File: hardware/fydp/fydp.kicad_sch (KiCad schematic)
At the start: 0 parts

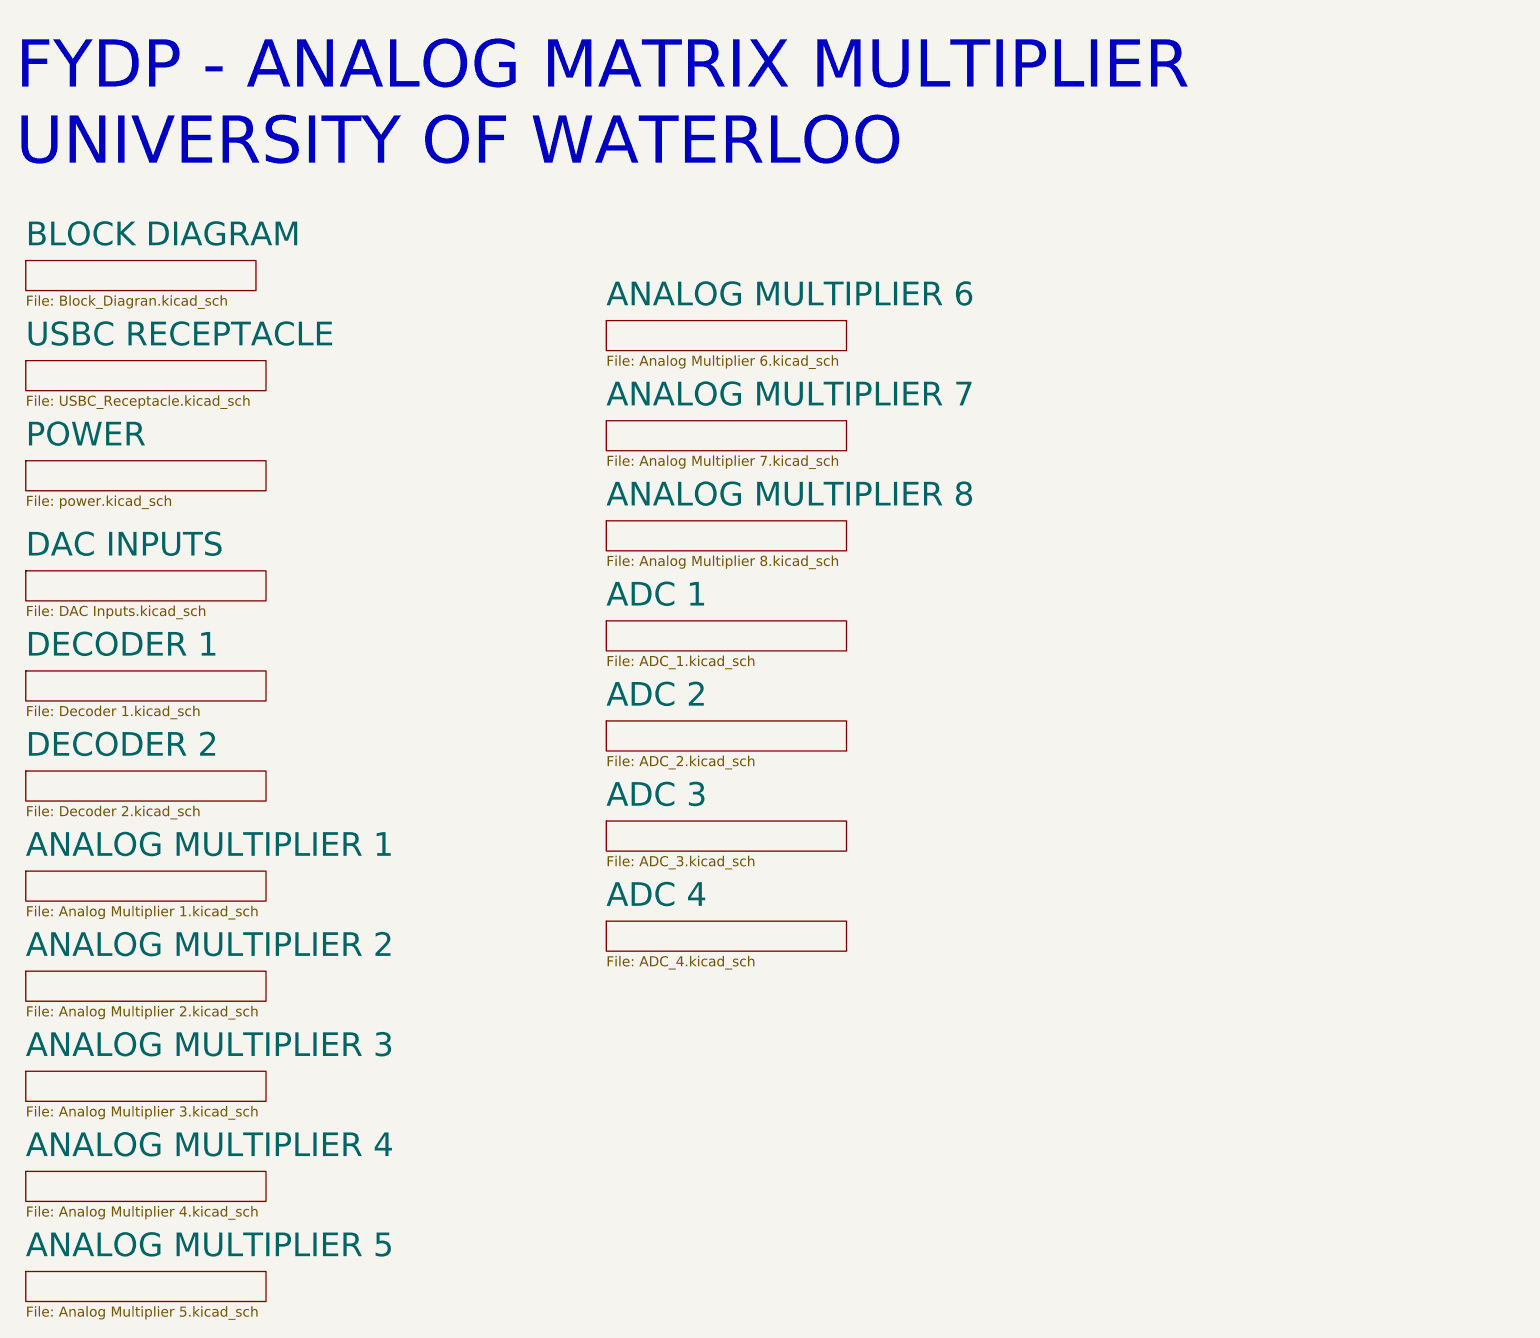
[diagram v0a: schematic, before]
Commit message: Remove 2 channels of multiplier and change ADC
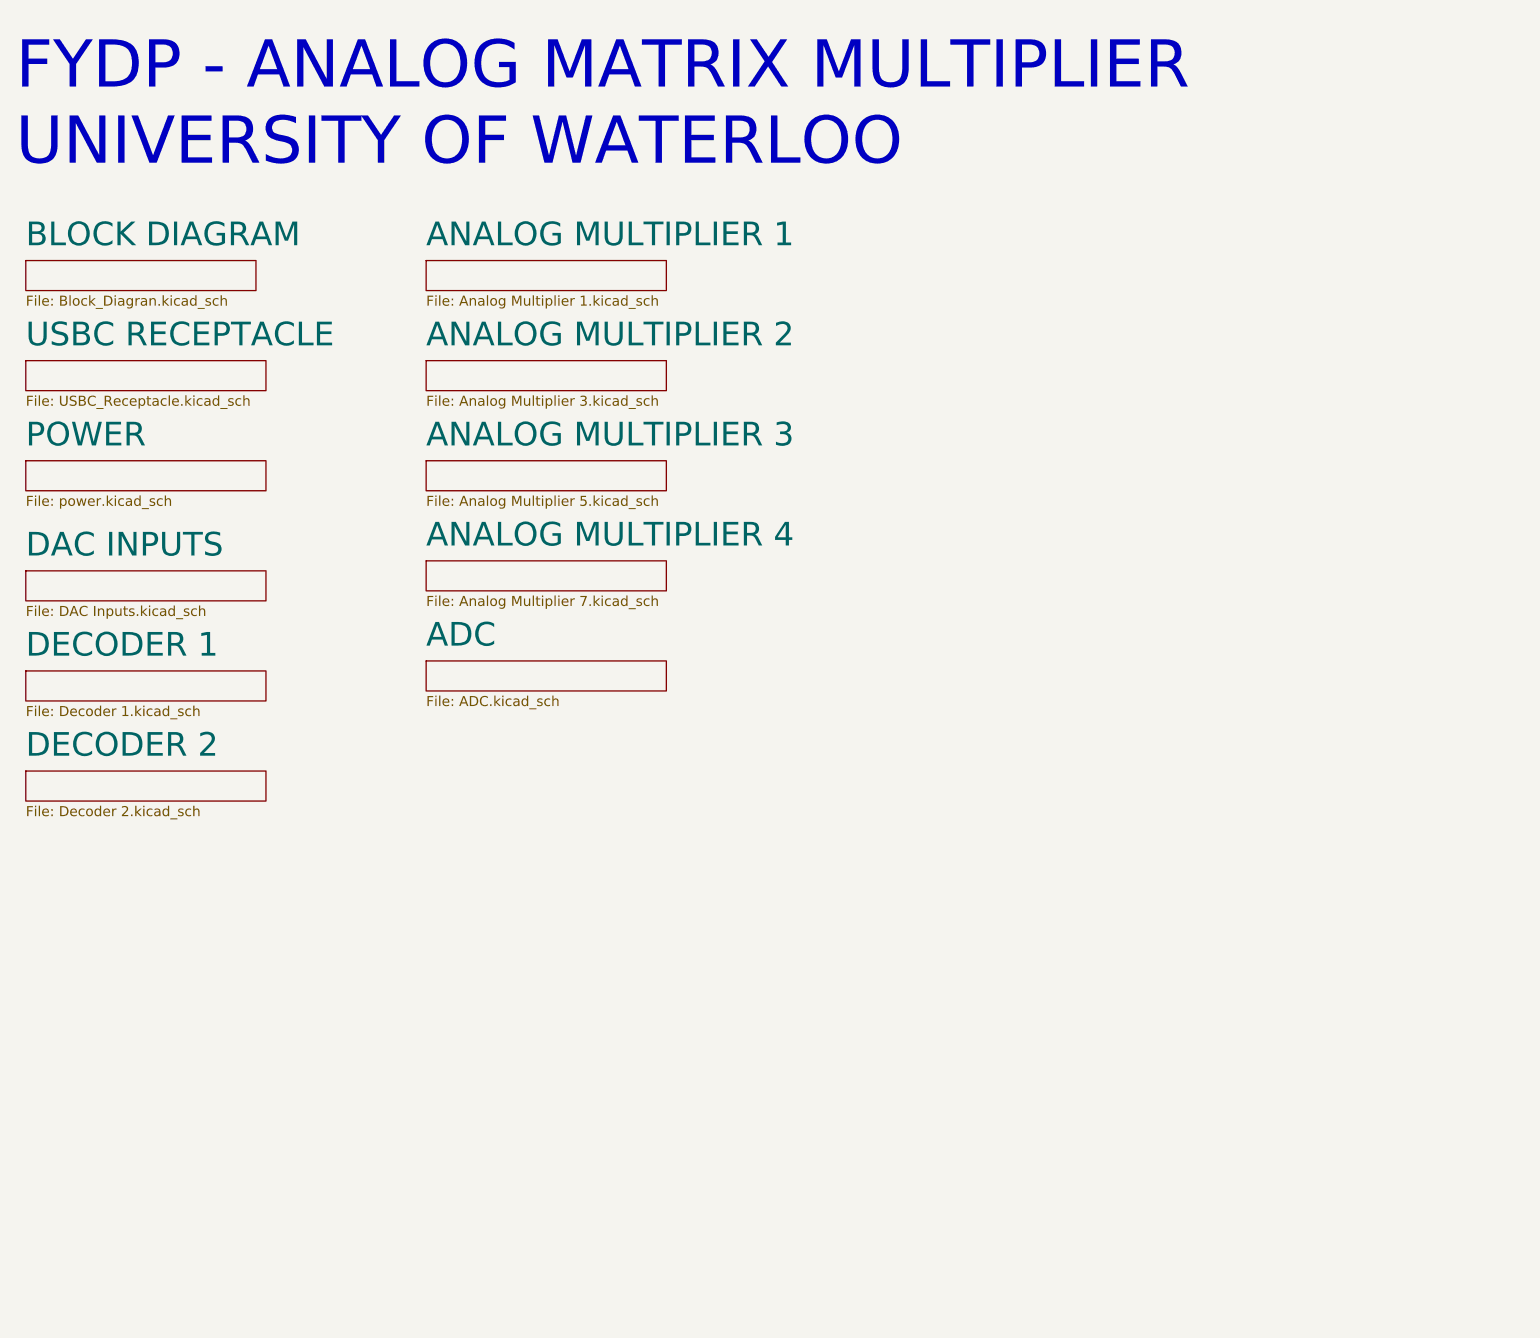
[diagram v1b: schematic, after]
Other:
- removed sheet ADC 1
- removed sheet ADC 2
- removed sheet ADC 3
- removed sheet ADC 4
- removed sheet ANALOG MULTIPLIER 5
- removed sheet ANALOG MULTIPLIER 6
- removed sheet ANALOG MULTIPLIER 7
- removed sheet ANALOG MULTIPLIER 8
- added sheet ADC (ADC.kicad_sch)
- sheet ANALOG MULTIPLIER 2: file Analog Multiplier 2.kicad_sch -> Analog Multiplier 3.kicad_sch
- sheet ANALOG MULTIPLIER 3: file Analog Multiplier 3.kicad_sch -> Analog Multiplier 5.kicad_sch
- sheet ANALOG MULTIPLIER 4: file Analog Multiplier 4.kicad_sch -> Analog Multiplier 7.kicad_sch
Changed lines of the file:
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@@
     (effects (font (size 6 6)) (justify left bottom))
-  )
-  (sheet (at 104.14 85.09) (size 30.48 3.81) (fields_autoplaced)
-    (stroke (width 0.1524) (type solid))
-    (fill (color 0 0 0 0.0000))
-    (property "Sheetname" "ANALOG MULTIPLIER 8" (at 104.14 83.5134 0)
-      (effects (font (size 3 3)) (justify left bottom))
-    )
-    (property "Sheetfile" "Analog Multiplier 8.kicad_sch" (at 104.14 89.4846 0)
-      (effects (font (size 1.27 1.27)) (justify left top))
-    )
-    (instances
-      (project "fydp"
-        (path "/2d5d1aad-2c7d-465e-90ef-822dec61a05e" (page "15"))
-      )
-    )
-  )
-  (sheet (at 104.14 123.19) (size 30.48 3.81) (fields_autoplaced)
-    (stroke (width 0.1524) (type solid))
-    (fill (color 0 0 0 0.0000))
-    (property "Sheetname" "ADC 3" (at 104.14 121.6134 0)
-      (effects (font (size 3 3)) (justify left bottom))
-    )
-    (property "Sheetfile" "ADC_3.kicad_sch" (at 104.14 127.5846 0)
-      (effects (font (size 1.27 1.27)) (justify left top))
-    )
-    (instances
-      (project "fydp"
-        (path "/2d5d1aad-2c7d-465e-90ef-822dec61a05e" (page "18"))
-      )
-    )
   )
   (sheet (at 30.48 52.07) (size 29.21 3.81) (fields_autoplaced)
@@
     )
   )
-  (sheet (at 30.48 129.54) (size 30.48 3.81) (fields_autoplaced)
+  (sheet (at 81.28 52.07) (size 30.48 3.81) (fields_autoplaced)
     (stroke (width 0.1524) (type solid))
     (fill (color 0 0 0 0.0000))
-    (property "Sheetname" "ANALOG MULTIPLIER 1" (at 30.48 127.9634 0)
+    (property "Sheetname" "ANALOG MULTIPLIER 1" (at 81.28 50.4934 0)
       (effects (font (size 3 3)) (justify left bottom))
     )
-    (property "Sheetfile" "Analog Multiplier 1.kicad_sch" (at 30.48 133.9346 0)
+    (property "Sheetfile" "Analog Multiplier 1.kicad_sch" (at 81.28 56.4646 0)
       (effects (font (size 1.27 1.27)) (justify left top))
     )
@@
       (project "fydp"
         (path "/2d5d1aad-2c7d-465e-90ef-822dec61a05e" (page "8"))
-      )
-    )
-  )
-  (sheet (at 104.14 110.49) (size 30.48 3.81) (fields_autoplaced)
-    (stroke (width 0.1524) (type solid))
-    (fill (color 0 0 0 0.0000))
-    (property "Sheetname" "ADC 2" (at 104.14 108.9134 0)
-      (effects (font (size 3 3)) (justify left bottom))
-    )
-    (property "Sheetfile" "ADC_2.kicad_sch" (at 104.14 114.8846 0)
-      (effects (font (size 1.27 1.27)) (justify left top))
-    )
-    (instances
-      (project "fydp"
-        (path "/2d5d1aad-2c7d-465e-90ef-822dec61a05e" (page "17"))
       )
     )
@@
     )
   )
-  (sheet (at 30.48 167.64) (size 30.48 3.81) (fields_autoplaced)
+  (sheet (at 81.28 90.17) (size 30.48 3.81) (fields_autoplaced)
     (stroke (width 0.1524) (type solid))
     (fill (color 0 0 0 0.0000))
-    (property "Sheetname" "ANALOG MULTIPLIER 4" (at 30.48 166.0634 0)
+    (property "Sheetname" "ANALOG MULTIPLIER 4" (at 81.28 88.5934 0)
       (effects (font (size 3 3)) (justify left bottom))
     )
-    (property "Sheetfile" "Analog Multiplier 4.kicad_sch" (at 30.48 172.0346 0)
+    (property "Sheetfile" "Analog Multiplier 7.kicad_sch" (at 81.28 94.5646 0)
       (effects (font (size 1.27 1.27)) (justify left top))
     )
@@
     )
   )
-  (sheet (at 30.48 142.24) (size 30.48 3.81) (fields_autoplaced)
+  (sheet (at 81.28 64.77) (size 30.48 3.81) (fields_autoplaced)
     (stroke (width 0.1524) (type solid))
     (fill (color 0 0 0 0.0000))
-    (property "Sheetname" "ANALOG MULTIPLIER 2" (at 30.48 140.6634 0)
+    (property "Sheetname" "ANALOG MULTIPLIER 2" (at 81.28 63.1934 0)
       (effects (font (size 3 3)) (justify left bottom))
     )
-    (property "Sheetfile" "Analog Multiplier 2.kicad_sch" (at 30.48 146.6346 0)
+    (property "Sheetfile" "Analog Multiplier 3.kicad_sch" (at 81.28 69.1646 0)
       (effects (font (size 1.27 1.27)) (justify left top))
     )
@@
     )
   )
-  (sheet (at 104.14 97.79) (size 30.48 3.81) (fields_autoplaced)
+  (sheet (at 81.28 102.87) (size 30.48 3.81) (fields_autoplaced)
     (stroke (width 0.1524) (type solid))
     (fill (color 0 0 0 0.0000))
-    (property "Sheetname" "ADC 1" (at 104.14 96.2134 0)
+    (property "Sheetname" "ADC" (at 81.28 101.2934 0)
       (effects (font (size 3 3)) (justify left bottom))
     )
-    (property "Sheetfile" "ADC_1.kicad_sch" (at 104.14 102.1846 0)
+    (property "Sheetfile" "ADC.kicad_sch" (at 81.28 107.2646 0)
       (effects (font (size 1.27 1.27)) (justify left top))
     )
     (instances
       (project "fydp"
-        (path "/2d5d1aad-2c7d-465e-90ef-822dec61a05e" (page "16"))
+        (path "/2d5d1aad-2c7d-465e-90ef-822dec61a05e" (page "12"))
       )
     )
   )
-  (sheet (at 104.14 72.39) (size 30.48 3.81) (fields_autoplaced)
+  (sheet (at 81.28 77.47) (size 30.48 3.81) (fields_autoplaced)
     (stroke (width 0.1524) (type solid))
     (fill (color 0 0 0 0.0000))
-    (property "Sheetname" "ANALOG MULTIPLIER 7" (at 104.14 70.8134 0)
+    (property "Sheetname" "ANALOG MULTIPLIER 3" (at 81.28 75.8934 0)
       (effects (font (size 3 3)) (justify left bottom))
     )
-    (property "Sheetfile" "Analog Multiplier 7.kicad_sch" (at 104.14 76.7846 0)
-      (effects (font (size 1.27 1.27)) (justify left top))
-    )
-    (instances
-      (project "fydp"
-        (path "/2d5d1aad-2c7d-465e-90ef-822dec61a05e" (page "14"))
-      )
-    )
-  )
-  (sheet (at 30.48 154.94) (size 30.48 3.81) (fields_autoplaced)
-    (stroke (width 0.1524) (type solid))
-    (fill (color 0 0 0 0.0000))
-    (property "Sheetname" "ANALOG MULTIPLIER 3" (at 30.48 153.3634 0)
-      (effects (font (size 3 3)) (justify left bottom))
-    )
-    (property "Sheetfile" "Analog Multiplier 3.kicad_sch" (at 30.48 159.3346 0)
+    (property "Sheetfile" "Analog Multiplier 5.kicad_sch" (at 81.28 81.8646 0)
       (effects (font (size 1.27 1.27)) (justify left top))
     )
@@
       (project "fydp"
         (path "/2d5d1aad-2c7d-465e-90ef-822dec61a05e" (page "10"))
-      )
-    )
-  )
-  (sheet (at 30.48 180.34) (size 30.48 3.81) (fields_autoplaced)
-    (stroke (width 0.1524) (type solid))
-    (fill (color 0 0 0 0.0000))
-    (property "Sheetname" "ANALOG MULTIPLIER 5" (at 30.48 178.7634 0)
-      (effects (font (size 3 3)) (justify left bottom))
-    )
-    (property "Sheetfile" "Analog Multiplier 5.kicad_sch" (at 30.48 184.7346 0)
-      (effects (font (size 1.27 1.27)) (justify left top))
-    )
-    (instances
-      (project "fydp"
-        (path "/2d5d1aad-2c7d-465e-90ef-822dec61a05e" (page "12"))
       )
     )
@@
       )
     )
-  )
-  (sheet (at 104.14 135.89) (size 30.48 3.81) (fields_autoplaced)
-    (stroke (width 0.1524) (type solid))
-    (fill (color 0 0 0 0.0000))
-    (property "Sheetname" "ADC 4" (at 104.14 134.3134 0)
-      (effects (font (size 3 3)) (justify left bottom))
-    )
-    (property "Sheetfile" "ADC_4.kicad_sch" (at 104.14 140.2846 0)
-      (effects (font (size 1.27 1.27)) (justify left top))
-    )
-    (instances
-      (project "fydp"
-        (path "/2d5d1aad-2c7d-465e-90ef-822dec61a05e" (page "19"))
-      )
-    )
-  )
-  (sheet (at 104.14 59.69) (size 30.48 3.81) (fields_autoplaced)
-    (stroke (width 0.1524) (type solid))
-    (fill (color 0 0 0 0.0000))
-    (property "Sheetname" "ANALOG MULTIPLIER 6" (at 104.14 58.1134 0)
-      (effects (font (size 3 3)) (justify left bottom))
-    )
-    (property "Sheetfile" "Analog Multiplier 6.kicad_sch" (at 104.14 64.0846 0)
-      (effects (font (size 1.27 1.27)) (justify left top))
-    )
-    (instances
-      (project "fydp"
-        (path "/2d5d1aad-2c7d-465e-90ef-822dec61a05e" (page "13"))
-      )
-    )
